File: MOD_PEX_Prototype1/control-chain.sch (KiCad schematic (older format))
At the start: 25 parts, among them J1 RJ45_CHAIN_MAIN, J2 RJ45_CHAIN_EXTENSION, Q1 MMBT3904, Q2 MMBT3906, U4 MAX13450E

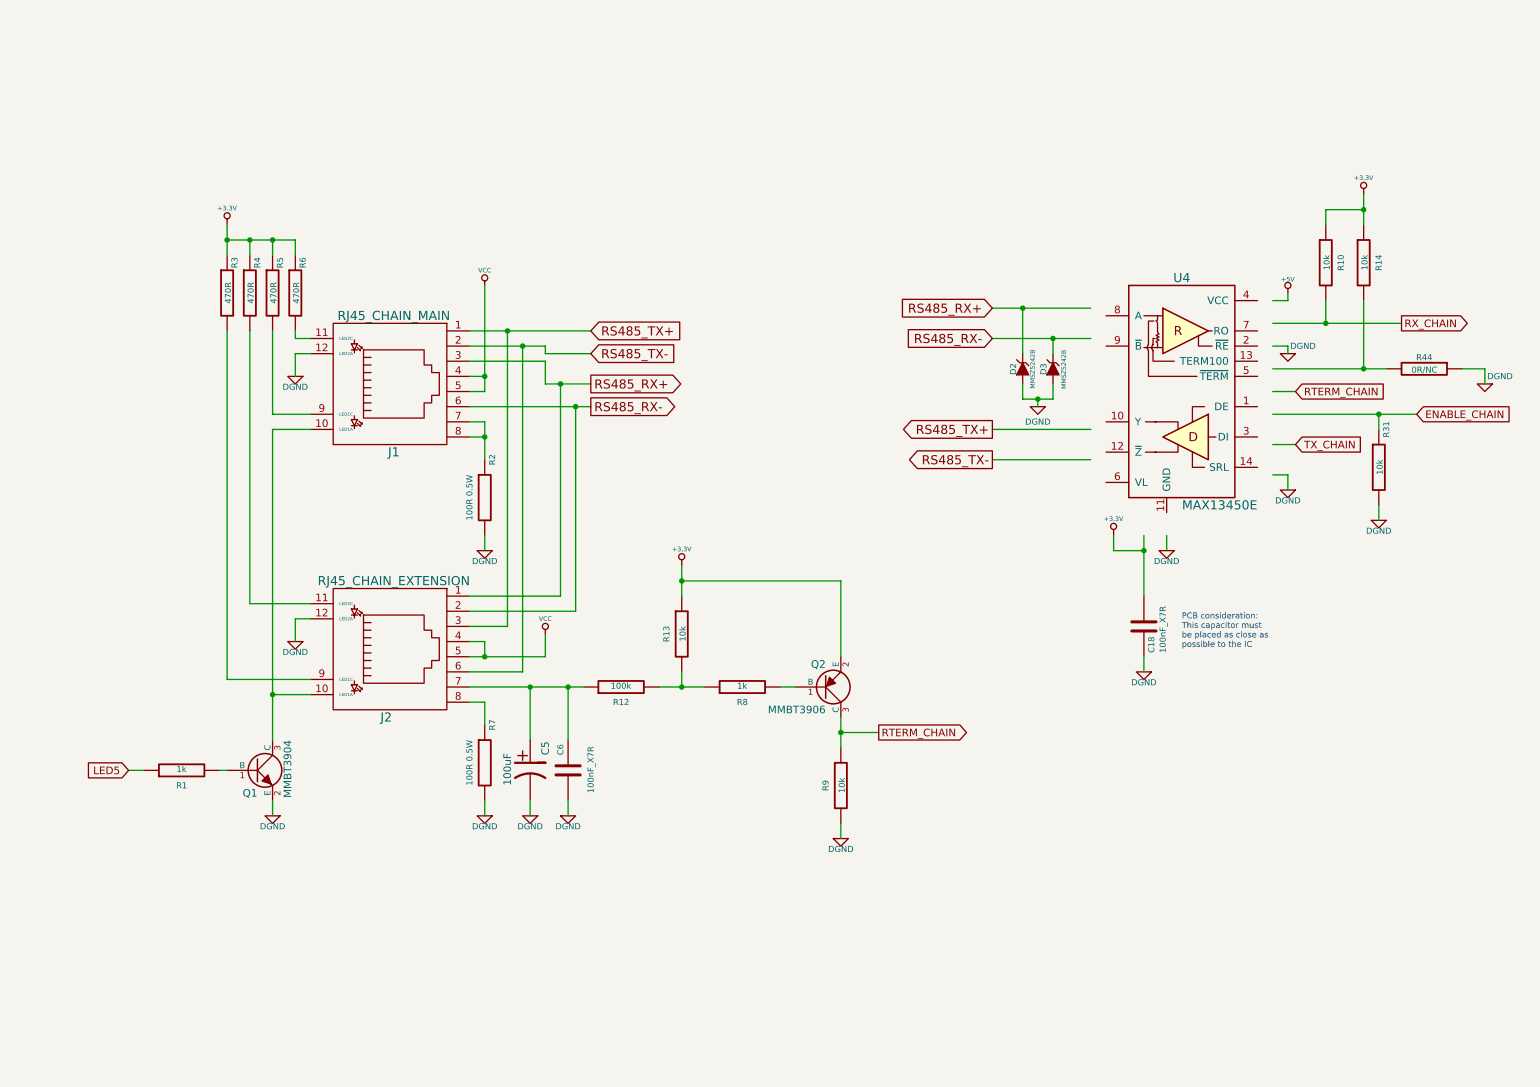
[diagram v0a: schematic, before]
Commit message: updating control chain circuit
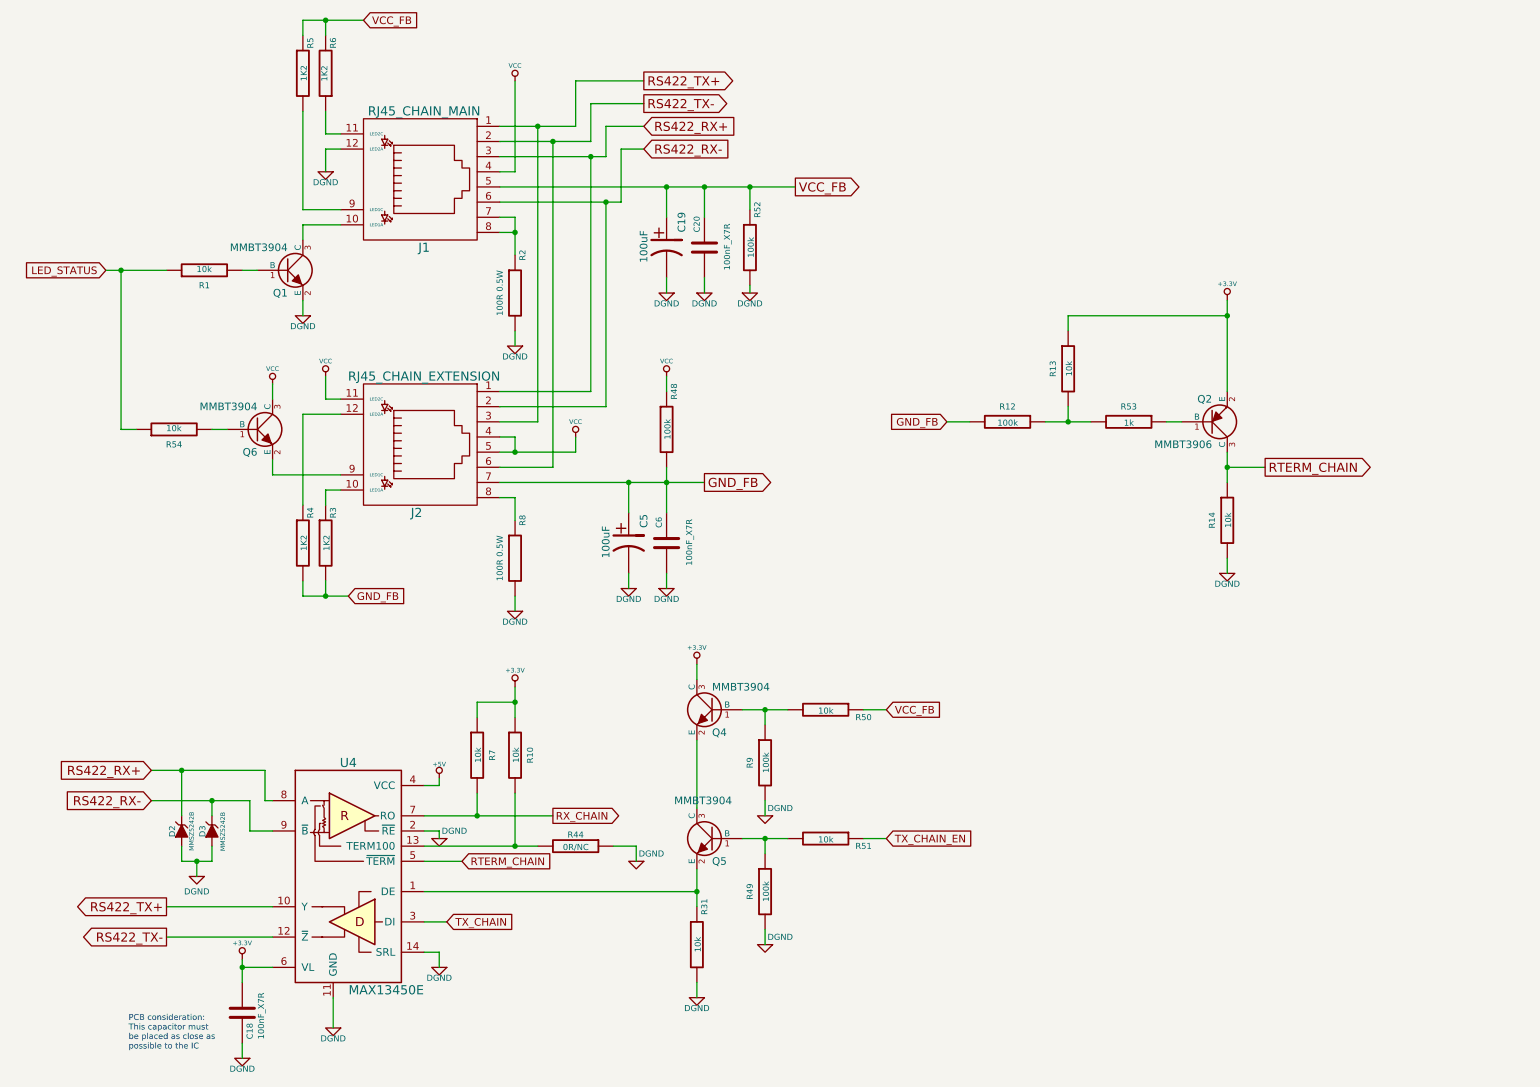
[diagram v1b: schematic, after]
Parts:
- added C19: 100uF, MOD_Footprints_Lib:CAP_RAD_5MM, symbol CP1
- added C20: 100nF_X7R, MOD_Footprints_Lib:SM0603, symbol C
- added Q4, Q5, Q6: MMBT3904, symbol MMBT3904
- added R48, R49, R52: 100k, MOD_Footprints_Lib:SM0603, symbol R
- added R50, R51, R54: 10k, MOD_Footprints_Lib:SM0603, symbol R
- added R53: 1k, MOD_Footprints_Lib:SM0603, symbol R
- Q1: footprint MOD_Footprints_Lib:SOT23 -> (none)
- R1: value 1k -> 10k
- R3, R4, R5, R6: value 470R -> 1K2
- R7: value 100R 0.5W -> 10k; footprint MOD_Footprints_Lib:SM1210 -> MOD_Footprints_Lib:SM0603
- R8: value 1k -> 100R 0.5W; footprint MOD_Footprints_Lib:SM0603 -> MOD_Footprints_Lib:SM1210
- R9: value 10k -> 100k
- U4: footprint MOD_Footprints_Lib:TSSOP14 -> TSSOP-14EP
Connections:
- net labels added: GND_FB, LED_STATUS, RS422_RX+, RS422_RX-, RS422_TX+, RS422_TX-, TX_CHAIN_EN, VCC_FB
- net labels removed: +3,3V, ENABLE_CHAIN, LED5, RS485_RX+, RS485_RX-, RS485_TX+, RS485_TX-
- wire segments 102 -> 133
